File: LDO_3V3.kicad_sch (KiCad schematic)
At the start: 0 parts

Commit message: progress on switch sheet
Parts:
- added C1101, C1102, C1103, C1104: 1uF, Capacitor_SMD:C_0603_1608Metric_Pad1.08x0.95mm_HandSolder, symbol Device:C_Small
- added C1105, C1106: 100nF, Capacitor_SMD:C_0603_1608Metric_Pad1.08x0.95mm_HandSolder, symbol Device:C_Small
- added U1101, U1102: MCP1703Ax-400xxMB, Package_TO_SOT_SMD:SOT-89-3, symbol Regulator_Linear:MCP1703Ax-400xxMB
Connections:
- net VIN: now also C1103.1, C1104.1, U1101.2 (VI), U1102.2 (VI)
- net VOUT: now also C1101.1, C1102.1, C1105.1, C1106.1, U1101.3 (VO), U1102.3 (VO)
- new net GND: C1101.2, C1102.2, C1103.2, C1104.2, C1105.2, C1106.2, U1101.1 (GND), U1102.1 (GND)
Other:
- note removed: "LDO"

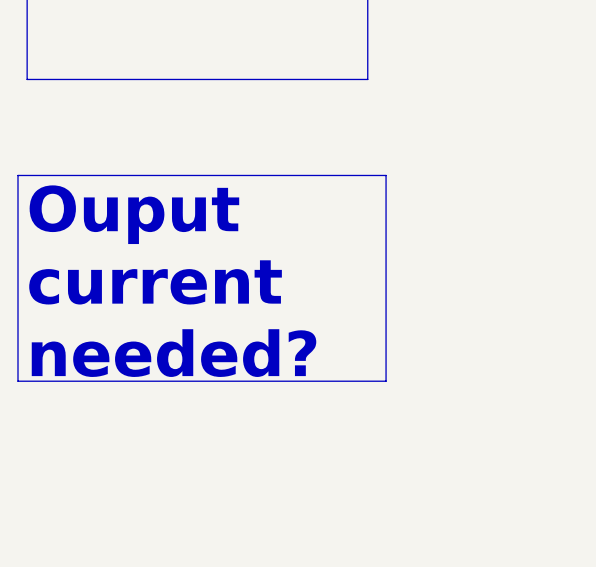
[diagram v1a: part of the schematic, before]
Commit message: specified parts and connection, updated notes
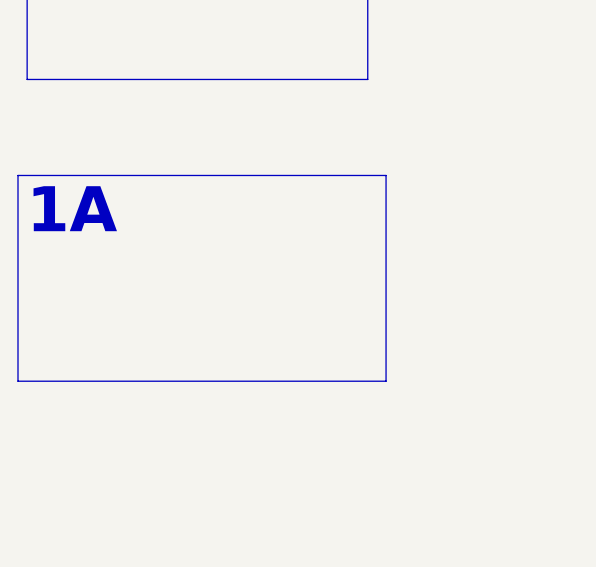
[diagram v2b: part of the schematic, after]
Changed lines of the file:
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@@
 		)
 	)
-	(text_box "Ouput current needed?"
+	(text_box "1A"
 		(exclude_from_sim no)
 		(at 25.146 74.168 0)

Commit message: specified design
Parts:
- removed C1101, C1102, C1103, C1104: 1uF, Capacitor_SMD:C_0603_1608Metric_Pad1.08x0.95mm_HandSolder, symbol Device:C_Small
- removed C1105, C1106: 100nF, Capacitor_SMD:C_0603_1608Metric_Pad1.08x0.95mm_HandSolder, symbol Device:C_Small
- removed U1101, U1102: MCP1703Ax-400xxMB, Package_TO_SOT_SMD:SOT-89-3, symbol Regulator_Linear:MCP1703Ax-400xxMB
- added C2001, C2002, C2003, C2004, C2005, C2006: C_Small, Capacitor_SMD:C_0603_1608Metric_Pad1.08x0.95mm_HandSolder, symbol Device:C_Small
- added C2007, C2008: 100n, Capacitor_SMD:C_0603_1608Metric_Pad1.08x0.95mm_HandSolder, symbol Device:C_Small
- added C2009, C2010, C2013, C2014: 1u, Capacitor_SMD:C_0603_1608Metric_Pad1.08x0.95mm_HandSolder, symbol Device:C_Small
- added C2011, C2012: 10u, Capacitor_SMD:C_0603_1608Metric_Pad1.08x0.95mm_HandSolder, symbol Device:C_Small
- added L2001, L2002: L_Small, Inductor_SMD:L_Taiyo-Yuden_NR-10050_9.8x10.0mm_HandSoldering, symbol Device:L_Small
- added Q2001, Q2002: NMOS, Package_TO_SOT_SMD:SOT-23-6, symbol Simulation_SPICE:NMOS
- added R2001, R2002, R2003, R2004, R2005, R2006: R_Small, Resistor_SMD:R_0603_1608Metric_Pad0.98x0.95mm_HandSolder, symbol Device:R_Small
- added U2001, U2002: TPS62933, Package_TO_SOT_SMD:SOT-583-8, symbol Regulator_Switching:TPS62933
- added U2003, U2004: LM74700, Package_TO_SOT_SMD:SOT-23-6, symbol Power_Management:LM74700
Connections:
- net GND: now also C2001.2, C2002.2, C2003.2, C2004.2, C2007.2, C2008.2, C2009.2, C2010.2, C2011.2, C2012.2, R2001.1, R2002.1, R2004.1, R2006.1, U2001.4 (GND), U2002.4 (GND), U2003.2 (GND), U2004.2 (GND)
- net VIN: now also C2003.1, C2004.1, U2001.2 (EN), U2001.3 (VIN), U2002.2 (EN), U2002.3 (VIN)
- net VOUT: now also Q2001.1 (D), Q2002.1 (D), U2003.4 (CATHODE), U2004.4 (CATHODE)
- new net: R2003.1, R2004.2, U2001.8 (FB)
- new net: C2007.1, C2009.1, C2011.1, C2013.1, L2001.2, Q2001.3 (S), R2003.2, U2003.3 (EN), U2003.6 (ANODE)
- new net: R2002.2, U2002.1 (RT)
- new net: R2001.2, U2001.1 (RT)
- new net: C2005.2, L2001.1, U2001.5 (SW)
- new net: C2005.1, U2001.6 (BST)
- new net: C2001.1, U2001.7 (SS)
- new net: C2013.2, U2003.1 (VCAP)
- new net: Q2001.2 (G), U2003.5 (GATE)
- new net: C2008.1, C2010.1, C2012.1, C2014.1, L2002.2, Q2002.3 (S), R2005.2, U2004.3 (EN), U2004.6 (ANODE)
- new net: C2006.2, L2002.1, U2002.5 (SW)
- new net: R2005.1, R2006.2, U2002.8 (FB)
- new net: C2014.2, U2004.1 (VCAP)
- new net: Q2002.2 (G), U2004.5 (GATE)
- new net: C2006.1, U2002.6 (BST)
- new net: C2002.1, U2002.7 (SS)
